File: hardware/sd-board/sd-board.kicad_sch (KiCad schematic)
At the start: 10 parts, among them J1 TF-01A push-push, J2 FPC 10P 0.5mm (IN), J3 FPC 10P 0.5mm (LCD), U1 74LVC1G04

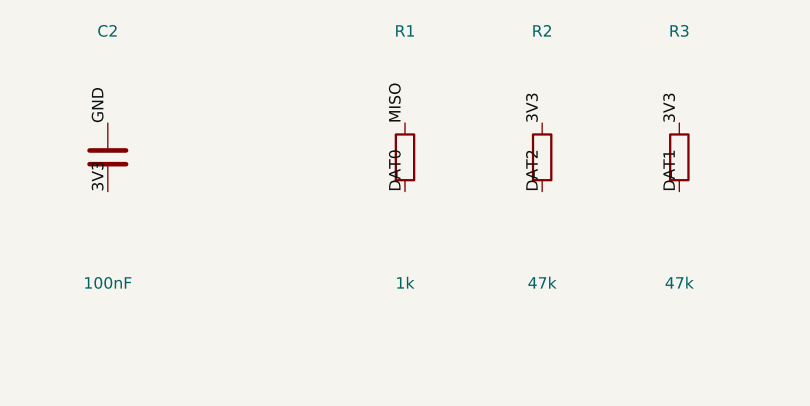
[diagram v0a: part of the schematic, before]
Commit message: feat(hardware): R1 220 ohm (C22962: the card reads at 20 MHz, the firmware keeps D/C high at idle), silkscreen 'LCD: gold UP' / 'IN: gold DOWN' (the double-sided sockets connect a turned-over cable mirrored); the 33 ohm and ESD parts listed for the re-route after the pin map
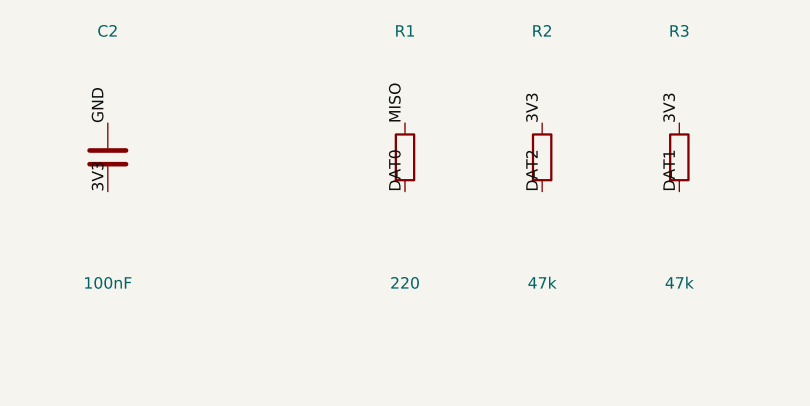
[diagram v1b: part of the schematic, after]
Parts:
- R1: value 1k -> 220; LCSC C21190 -> C22962
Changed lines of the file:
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@@
 (label "3V3" (at 66.04 60.96 90) (effects (font (size 1.27 1.27)) (justify left bottom)))
 (no_connect (at 63.5 68.58))
-(symbol (lib_id "Device:R") (at 109.22 124.46 0) (unit 1) (exclude_from_sim no) (in_bom yes) (on_board yes) (dnp no) (property "Reference" "R1" (at 109.22 110.46 0) (effects (font (size 1.27 1.27)))) (property "Value" "1k" (at 109.22 138.45999999999998 0) (effects (font (size 1.27 1.27)))) (property "Footprint" "sdboard:R0603" (at 109.22 124.46 0) (effects (font (size 1.27 1.27)) (hide yes))) (property "Datasheet" "" (at 109.22 124.46 0) (effects (font (size 1.27 1.27)) (hide yes))) (property "LCSC" "C21190" (at 109.22 124.46 0) (effects (font (size 1.27 1.27)) (hide yes))) (pin "1") (pin "2") (instances (project "sd-board" (path "/766c70bd-1acb-59f5-b703-96c0315a8041" (reference "R1") (unit 1)))))
+(symbol (lib_id "Device:R") (at 109.22 124.46 0) (unit 1) (exclude_from_sim no) (in_bom yes) (on_board yes) (dnp no) (property "Reference" "R1" (at 109.22 110.46 0) (effects (font (size 1.27 1.27)))) (property "Value" "220" (at 109.22 138.45999999999998 0) (effects (font (size 1.27 1.27)))) (property "Footprint" "sdboard:R0603" (at 109.22 124.46 0) (effects (font (size 1.27 1.27)) (hide yes))) (property "Datasheet" "" (at 109.22 124.46 0) (effects (font (size 1.27 1.27)) (hide yes))) (property "LCSC" "C22962" (at 109.22 124.46 0) (effects (font (size 1.27 1.27)) (hide yes))) (pin "1") (pin "2") (instances (project "sd-board" (path "/766c70bd-1acb-59f5-b703-96c0315a8041" (reference "R1") (unit 1)))))
 (label "MISO" (at 109.22 120.65 90) (effects (font (size 1.27 1.27)) (justify left bottom)))
 (label "DAT0" (at 109.22 128.27 270) (effects (font (size 1.27 1.27)) (justify left bottom)))

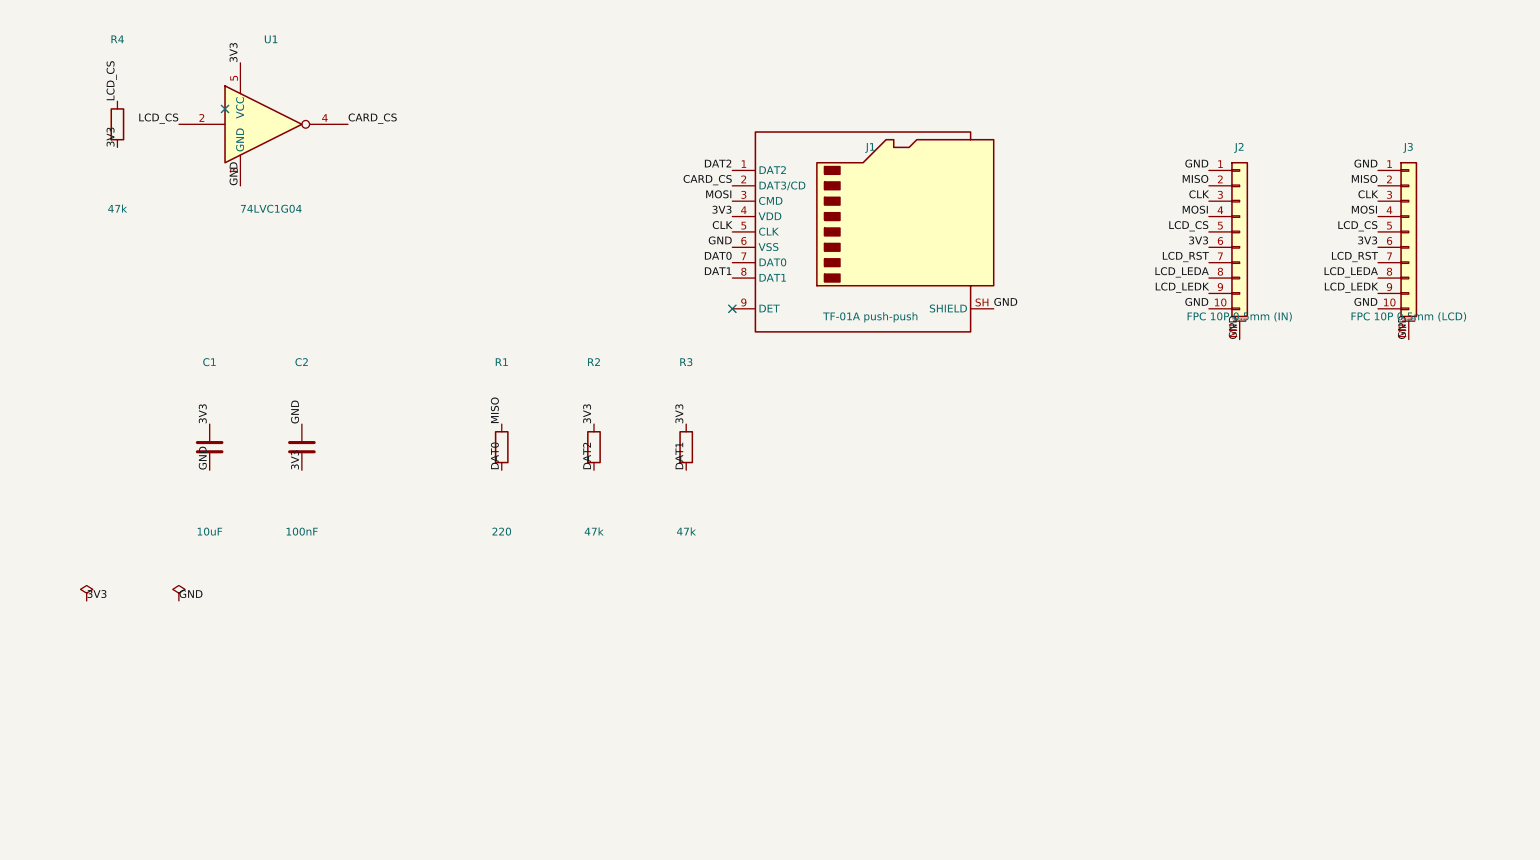
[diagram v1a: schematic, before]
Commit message: feat(sd-board): v6, rerouted to J12's probed pin map (2 PC8, 3 PC7 CS, 4 PC9 CLK, 5 PC10 MOSI, 7 3.3 V to confirm): J3 single-sided top contact (C3446068, wired by place), R4 a pull-down, R1/R5/R6 100 ohm (R5, R6 in series on CLK and MOSI at the column's top), the column in J2's order with a ground guard lane between CS and CLK, CS across on the bottom, U1/R2/R4/C2 off the tray's lips (asserted); DRC 0, nets 48 = 48. Not ready to order: pin 7, the mirror check (J2's face), the ESD (USBLC6-2SC6 is two lines: USBLC6-4SC6 not placed yet)
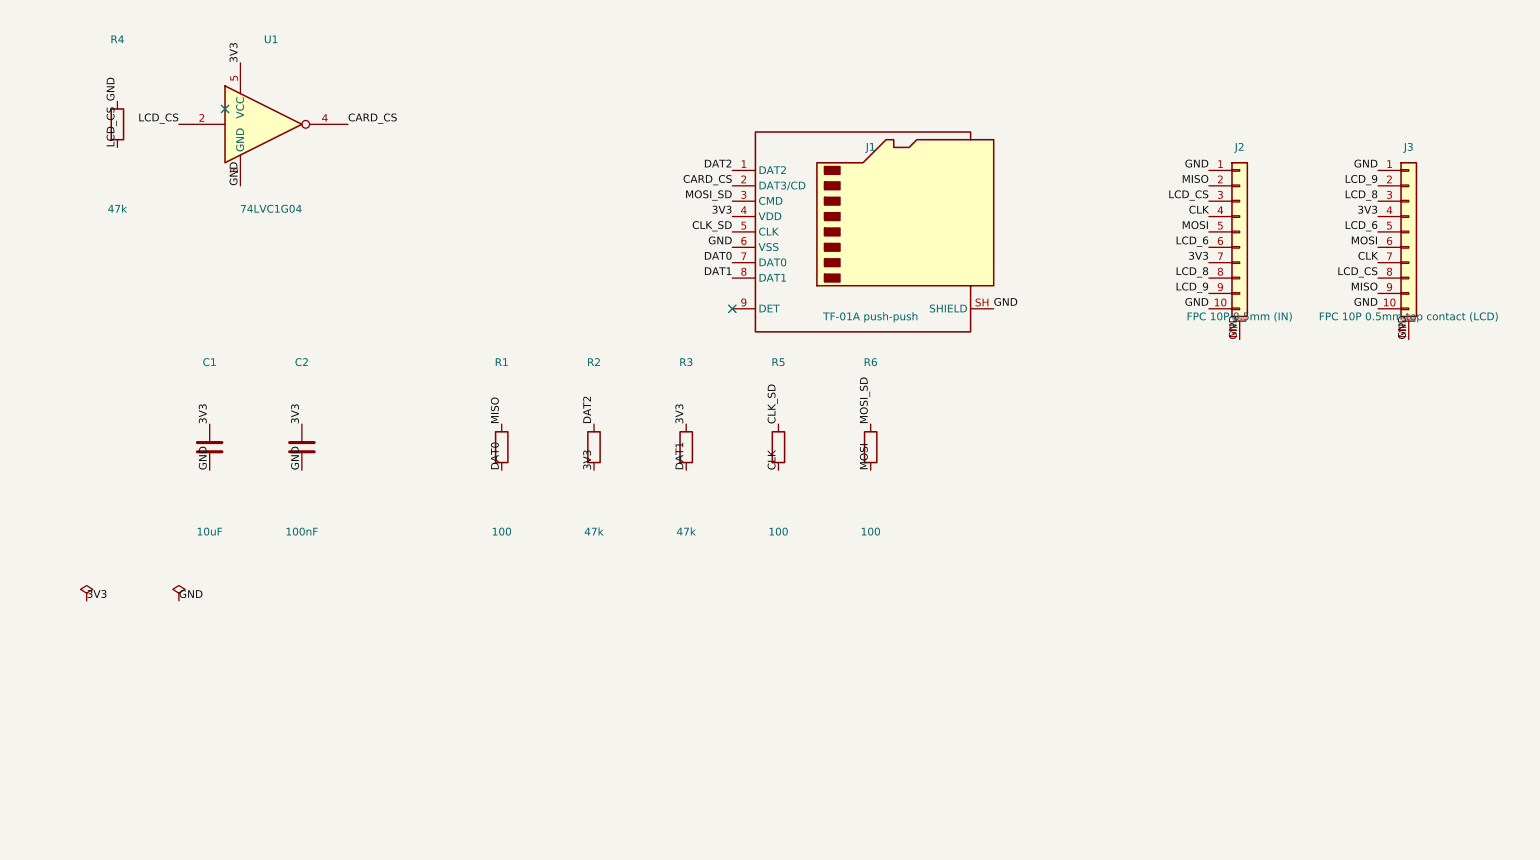
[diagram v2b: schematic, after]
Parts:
- added R5, R6: 100, sdboard:R0603, symbol Device:R
- J3: value FPC 10P 0.5mm (LCD) -> FPC 10P 0.5mm top contact (LCD); footprint sdboard:FPC-SMD_10P-P0.50_HC-FPC-05-09-10RLTAG -> sdboard:FPC-SMD_10P-P0.50_XUNPU_FPC-0.5AS-10PWBH20; LCSC C5213750 -> C3446068
- R1: value 220 -> 100; LCSC C22962 -> C22775
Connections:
- net 3V3: now also C2.1, J2.7 (Pin_7), J3.4 (Pin_4), R2.2; no longer C2.2, J2.6 (Pin_6), J3.6 (Pin_6), R2.1, R4.2
- net CLK: now also J2.4 (Pin_4), J3.7 (Pin_7), R5.2; no longer J1.5 (CLK), J2.3 (Pin_3), J3.3 (Pin_3)
- net DAT2: now also R2.1; no longer R2.2
- net GND: now also C2.2, R4.1; no longer C2.1
- net LCD_CS: now also J2.3 (Pin_3), J3.8 (Pin_8), R4.2; no longer J2.5 (Pin_5), J3.5 (Pin_5), R4.1
- net MISO: now also J3.9 (Pin_9); no longer J3.2 (Pin_2)
- net MOSI: now also J2.5 (Pin_5), J3.6 (Pin_6), R6.2; no longer J1.3 (CMD), J2.4 (Pin_4), J3.4 (Pin_4)
- net LCD_LEDA renamed LCD_8
- net LCD_8: now also J3.3 (Pin_3); no longer J3.8 (Pin_8)
- net LCD_LEDK renamed LCD_9
- net LCD_9: now also J3.2 (Pin_2); no longer J3.9 (Pin_9)
- removed net LCD_RST: J2.7 (Pin_7), J3.7 (Pin_7)
- new net CLK_SD: J1.5 (CLK), R5.1
- new net LCD_6: J2.6 (Pin_6), J3.5 (Pin_5)
- new net MOSI_SD: J1.3 (CMD), R6.1

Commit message: feat(sd-board): ESD (two USBLC6-2SC6, C7519, every card line straight through a column: no stub), the swap block (Julius's idea: each line DO, CS, CLK, DI, 3V3 through a bridged solder jumper between J2 and the SD part: cut and wire to fix a wrong J12 guess) and test pads on J12's unprobed pins 6, 8, 9 and GND; DRC 0, nets 74 = 74; READMEs: the ESD is no longer open
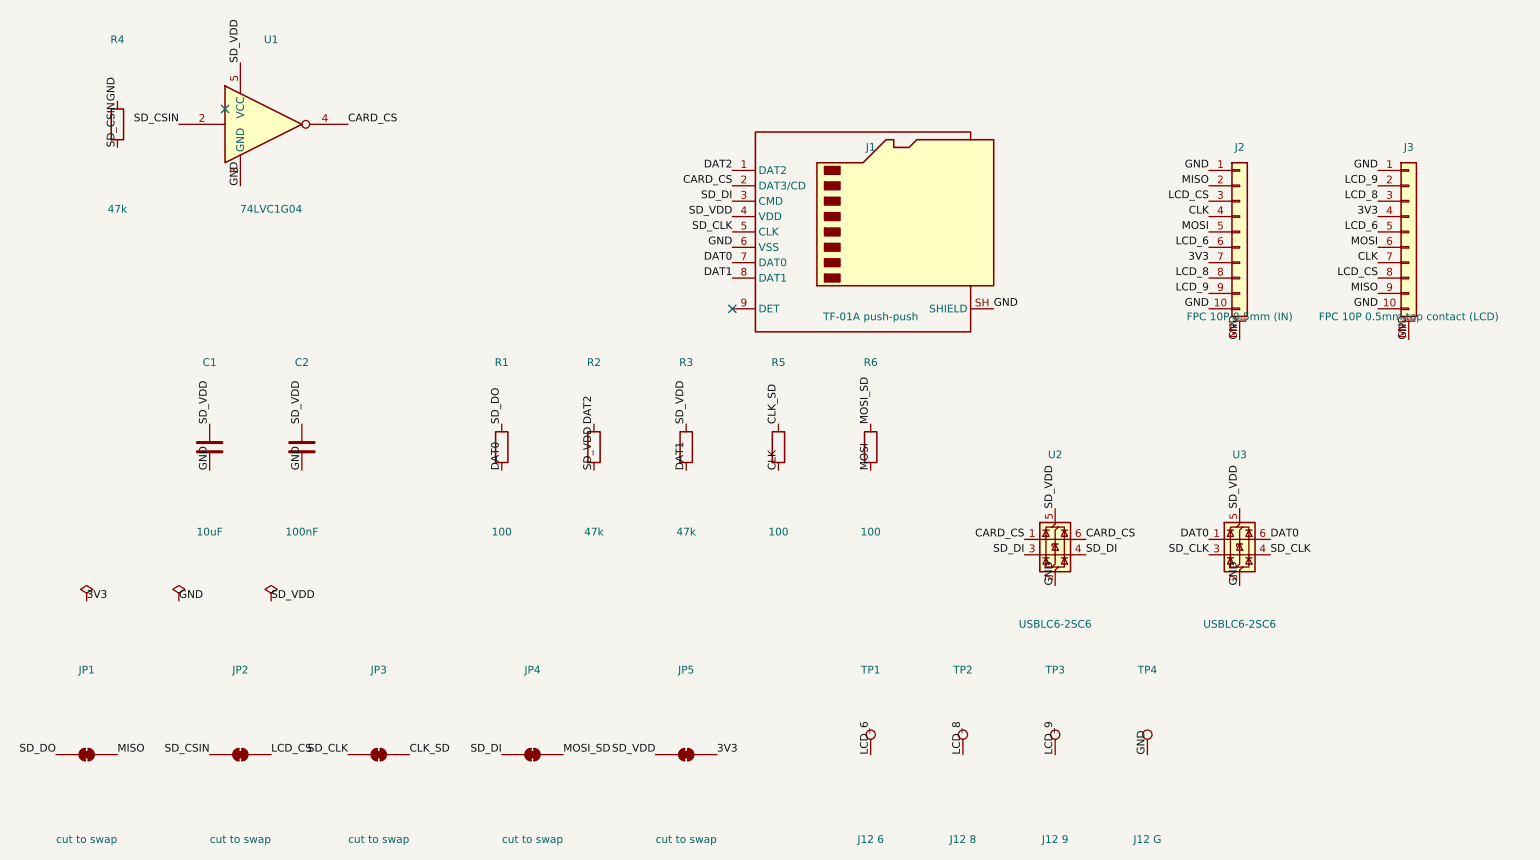
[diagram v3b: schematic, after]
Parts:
- added JP1, JP2, JP3, JP4, JP5: cut to swap, Jumper:SolderJumper-2_P1.3mm_Bridged_RoundedPad1.0x1.5mm, symbol Jumper:SolderJumper_2_Bridged
- added TP1: J12 6, TestPoint:TestPoint_Pad_D1.0mm, symbol Connector:TestPoint
- added TP2: J12 8, TestPoint:TestPoint_Pad_D1.0mm, symbol Connector:TestPoint
- added TP3: J12 9, TestPoint:TestPoint_Pad_D1.0mm, symbol Connector:TestPoint
- added TP4: J12 G, TestPoint:TestPoint_Pad_D1.0mm, symbol Connector:TestPoint
- added U2, U3: USBLC6-2SC6, sdboard:SOT-23-6_L2.9-W1.6-P0.95-LS2.8-BL, symbol Power_Protection:USBLC6-2P6
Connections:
- net 3V3: now also JP5.2 (B); no longer C1.1, C2.1, J1.4 (VDD), R2.2, R3.1, U1.5 (VCC)
- net CARD_CS: now also U2.1 (I/O1), U2.6 (I/O1)
- net CLK_SD: now also JP3.2 (B); no longer J1.5 (CLK)
- net DAT0: now also U3.1 (I/O1), U3.6 (I/O1)
- net GND: now also TP4.1, U2.2 (GND), U3.2 (GND)
- net LCD_6: now also TP1.1
- net LCD_8: now also TP2.1
- net LCD_9: now also TP3.1
- net LCD_CS: now also JP2.2 (B); no longer R4.2, U1.2
- net MISO: now also JP1.2 (B); no longer R1.1
- net MOSI_SD: now also JP4.2 (B); no longer J1.3 (CMD)
- new net SD_CLK: J1.5 (CLK), JP3.1 (A), U3.3 (I/O2), U3.4 (I/O2)
- new net SD_CSIN: JP2.1 (A), R4.2, U1.2
- new net SD_DI: J1.3 (CMD), JP4.1 (A), U2.3 (I/O2), U2.4 (I/O2)
- new net SD_DO: JP1.1 (A), R1.1
- new net SD_VDD: C1.1, C2.1, J1.4 (VDD), JP5.1 (A), R2.2, R3.1, U1.5 (VCC), U2.5 (VBUS), U3.5 (VBUS)

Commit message: feat(sd-board): the swap jumpers bigger (own footprint: 1.5 x 2 mm pads 3 mm apart, a 1.5 mm bare bridge to cut), J12's pin number right of each J12-side pad, the test pads 1.5 mm; DRC 0, nets 74 = 74
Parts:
- JP1, JP2, JP3, JP4, JP5: footprint Jumper:SolderJumper-2_P1.3mm_Bridged_RoundedPad1.0x1.5mm -> sdboard:SolderJumper-2_Cut_P3.0mm_Pad1.5x2.0mm
- TP1, TP2, TP3, TP4: footprint TestPoint:TestPoint_Pad_D1.0mm -> TestPoint:TestPoint_Pad_D1.5mm

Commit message: fix(sd-board): Julius's prototype review: R1 220 Ohm (C22962: a card left in SPI mode against D/C, 15 mA not 33), R5/R6 510 Ohm (C23193: the stock screen blank with a native-mode card at CLK direct, fine at 510), R7 47k DAT0 pull-up, FB1 ferrite (C1002) from JP5 to the card's supply and C3 100 nF on its VDD line, TP5 on the socket's DET; DRC 0, nets 82 = 82, mockups regenerated (0 open edges); README: must-pass cold-boot bench test with stock and SLOOP, hot insertion, J3's numbering check; SD-CARD-DESIGN: the prototype's measurements, the R1 timing trade
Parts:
- added C3: 100nF, sdboard:C0603, symbol Device:C
- added FB1: 600R@100MHz, sdboard:R0603, symbol Device:FerriteBead
- added R7: 47k, sdboard:R0603, symbol Device:R
- added TP5: J12 DET, TestPoint:TestPoint_Pad_D1.5mm, symbol Connector:TestPoint
- R1: value 100 -> 220; LCSC C22775 -> C22962
- R5, R6: value 100 -> 510; LCSC C22775 -> C23193
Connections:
- net DAT0: now also R7.2
- net GND: now also C3.2
- net SD_VDD: now also C3.1, FB1.2, R7.1; no longer JP5.1 (A)
- net CARD_DET: now reaches J1.9 (DET)
- net CARD_DET: now also TP5.1
- new net SD_VIN: FB1.1, JP5.1 (A)
- no-connect marks 2 -> 1

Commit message: feat(sd-board): R1, R5, R6 on 0603 hand-solder pads (Julius: leave room to retune them; same JLC parts), the README's retuning guide (up if the screen misbehaves with a card in, down if 20 MHz shows CRC errors; no trimmers on a clock line); DRC 0, nets 82 = 82, mockups regenerated (0 open edges)
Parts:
- R1, R5, R6: footprint sdboard:R0603 -> Resistor_SMD:R_0603_1608Metric_Pad0.98x0.95mm_HandSolder
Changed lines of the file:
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@@
 (label "SD_VDD" (at 66.04 60.96 90) (effects (font (size 1.27 1.27)) (justify left bottom)))
 (no_connect (at 63.5 68.58))
-(symbol (lib_id "Device:R") (at 109.22 124.46 0) (unit 1) (exclude_from_sim no) (in_bom yes) (on_board yes) (dnp no) (property "Reference" "R1" (at 109.22 110.46 0) (effects (font (size 1.27 1.27)))) (property "Value" "220" (at 109.22 138.45999999999998 0) (effects (font (size 1.27 1.27)))) (property "Footprint" "sdboard:R0603" (at 109.22 124.46 0) (effects (font (size 1.27 1.27)) (hide yes))) (property "Datasheet" "" (at 109.22 124.46 0) (effects (font (size 1.27 1.27)) (hide yes))) (property "LCSC" "C22962" (at 109.22 124.46 0) (effects (font (size 1.27 1.27)) (hide yes))) (pin "1") (pin "2") (instances (project "sd-board" (path "/766c70bd-1acb-59f5-b703-96c0315a8041" (reference "R1") (unit 1)))))
+(symbol (lib_id "Device:R") (at 109.22 124.46 0) (unit 1) (exclude_from_sim no) (in_bom yes) (on_board yes) (dnp no) (property "Reference" "R1" (at 109.22 110.46 0) (effects (font (size 1.27 1.27)))) (property "Value" "220" (at 109.22 138.45999999999998 0) (effects (font (size 1.27 1.27)))) (property "Footprint" "Resistor_SMD:R_0603_1608Metric_Pad0.98x0.95mm_HandSolder" (at 109.22 124.46 0) (effects (font (size 1.27 1.27)) (hide yes))) (property "Datasheet" "" (at 109.22 124.46 0) (effects (font (size 1.27 1.27)) (hide yes))) (property "LCSC" "C22962" (at 109.22 124.46 0) (effects (font (size 1.27 1.27)) (hide yes))) (pin "1") (pin "2") (instances (project "sd-board" (path "/766c70bd-1acb-59f5-b703-96c0315a8041" (reference "R1") (unit 1)))))
 (label "SD_DO" (at 109.22 120.65 90) (effects (font (size 1.27 1.27)) (justify left bottom)))
 (label "DAT0" (at 109.22 128.27 270) (effects (font (size 1.27 1.27)) (justify left bottom)))
@@
 (label "GND" (at 45.72 67.31 90) (effects (font (size 1.27 1.27)) (justify left bottom)))
 (label "SD_CSIN" (at 45.72 74.93 270) (effects (font (size 1.27 1.27)) (justify left bottom)))
-(symbol (lib_id "Device:R") (at 154.94 124.46 0) (unit 1) (exclude_from_sim no) (in_bom yes) (on_board yes) (dnp no) (property "Reference" "R5" (at 154.94 110.46 0) (effects (font (size 1.27 1.27)))) (property "Value" "510" (at 154.94 138.45999999999998 0) (effects (font (size 1.27 1.27)))) (property "Footprint" "sdboard:R0603" (at 154.94 124.46 0) (effects (font (size 1.27 1.27)) (hide yes))) (property "Datasheet" "" (at 154.94 124.46 0) (effects (font (size 1.27 1.27)) (hide yes))) (property "LCSC" "C23193" (at 154.94 124.46 0) (effects (font (size 1.27 1.27)) (hide yes))) (pin "1") (pin "2") (instances (project "sd-board" (path "/766c70bd-1acb-59f5-b703-96c0315a8041" (reference "R5") (unit 1)))))
+(symbol (lib_id "Device:R") (at 154.94 124.46 0) (unit 1) (exclude_from_sim no) (in_bom yes) (on_board yes) (dnp no) (property "Reference" "R5" (at 154.94 110.46 0) (effects (font (size 1.27 1.27)))) (property "Value" "510" (at 154.94 138.45999999999998 0) (effects (font (size 1.27 1.27)))) (property "Footprint" "Resistor_SMD:R_0603_1608Metric_Pad0.98x0.95mm_HandSolder" (at 154.94 124.46 0) (effects (font (size 1.27 1.27)) (hide yes))) (property "Datasheet" "" (at 154.94 124.46 0) (effects (font (size 1.27 1.27)) (hide yes))) (property "LCSC" "C23193" (at 154.94 124.46 0) (effects (font (size 1.27 1.27)) (hide yes))) (pin "1") (pin "2") (instances (project "sd-board" (path "/766c70bd-1acb-59f5-b703-96c0315a8041" (reference "R5") (unit 1)))))
 (label "CLK_SD" (at 154.94 120.65 90) (effects (font (size 1.27 1.27)) (justify left bottom)))
 (label "CLK" (at 154.94 128.27 270) (effects (font (size 1.27 1.27)) (justify left bottom)))
-(symbol (lib_id "Device:R") (at 170.18 124.46 0) (unit 1) (exclude_from_sim no) (in_bom yes) (on_board yes) (dnp no) (property "Reference" "R6" (at 170.18 110.46 0) (effects (font (size 1.27 1.27)))) (property "Value" "510" (at 170.18 138.45999999999998 0) (effects (font (size 1.27 1.27)))) (property "Footprint" "sdboard:R0603" (at 170.18 124.46 0) (effects (font (size 1.27 1.27)) (hide yes))) (property "Datasheet" "" (at 170.18 124.46 0) (effects (font (size 1.27 1.27)) (hide yes))) (property "LCSC" "C23193" (at 170.18 124.46 0) (effects (font (size 1.27 1.27)) (hide yes))) (pin "1") (pin "2") (instances (project "sd-board" (path "/766c70bd-1acb-59f5-b703-96c0315a8041" (reference "R6") (unit 1)))))
+(symbol (lib_id "Device:R") (at 170.18 124.46 0) (unit 1) (exclude_from_sim no) (in_bom yes) (on_board yes) (dnp no) (property "Reference" "R6" (at 170.18 110.46 0) (effects (font (size 1.27 1.27)))) (property "Value" "510" (at 170.18 138.45999999999998 0) (effects (font (size 1.27 1.27)))) (property "Footprint" "Resistor_SMD:R_0603_1608Metric_Pad0.98x0.95mm_HandSolder" (at 170.18 124.46 0) (effects (font (size 1.27 1.27)) (hide yes))) (property "Datasheet" "" (at 170.18 124.46 0) (effects (font (size 1.27 1.27)) (hide yes))) (property "LCSC" "C23193" (at 170.18 124.46 0) (effects (font (size 1.27 1.27)) (hide yes))) (pin "1") (pin "2") (instances (project "sd-board" (path "/766c70bd-1acb-59f5-b703-96c0315a8041" (reference "R6") (unit 1)))))
 (label "MOSI_SD" (at 170.18 120.65 90) (effects (font (size 1.27 1.27)) (justify left bottom)))
 (label "MOSI" (at 170.18 128.27 270) (effects (font (size 1.27 1.27)) (justify left bottom)))
